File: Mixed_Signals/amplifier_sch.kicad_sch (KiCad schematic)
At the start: 6 parts, among them J1 audio connector, U1 ${SIM.PARAMS}

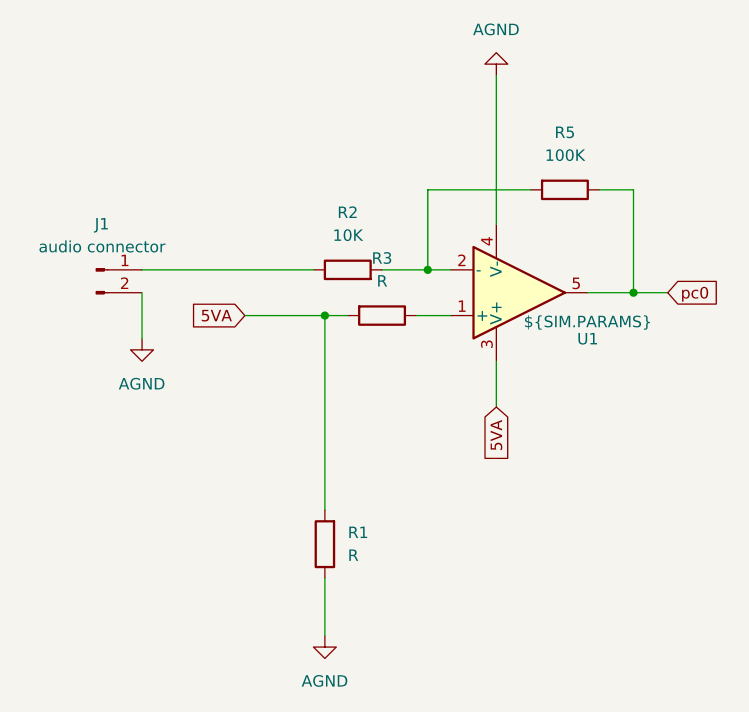
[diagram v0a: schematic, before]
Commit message: Fixed voltage divider error
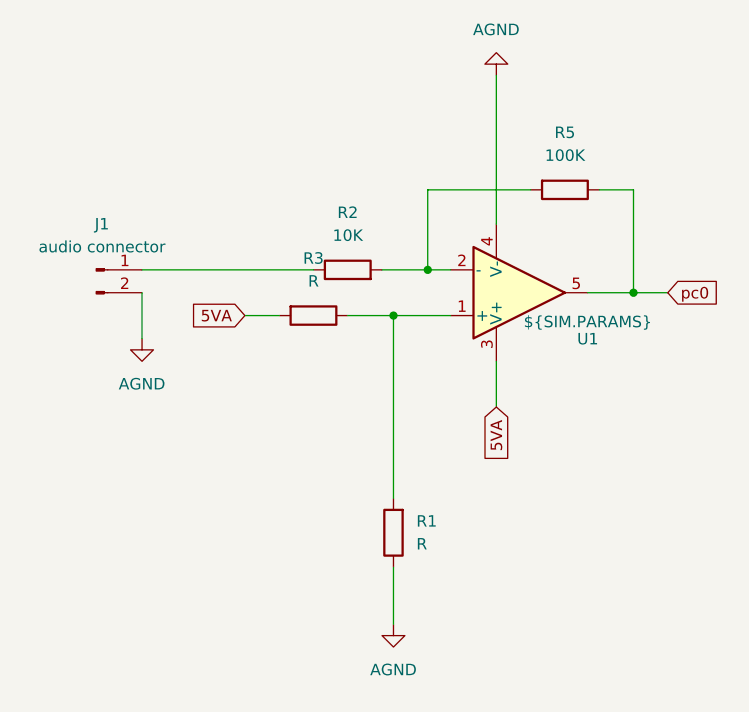
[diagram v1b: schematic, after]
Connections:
- net 5VA: no longer R1.2
- net at R3.1, U1.1 (+): now also R1.2
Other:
- moved on the sheet: R1, R3
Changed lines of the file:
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@@
 	(paper "A4")
 	(junction
-		(at 106.68 95.25)
+		(at 114.3 95.25)
 		(diameter 0)
 		(color 0 0 0 0)
@@
 	(wire
 		(pts
-			(xy 109.22 95.25) (xy 106.68 95.25)
-		)
-		(stroke
-			(width 0)
-			(type default)
-		)
-	)
-	(wire
-		(pts
 			(xy 125.73 85.09) (xy 125.73 68.58)
 		)
@@
 	(wire
 		(pts
-			(xy 116.84 95.25) (xy 120.65 95.25)
+			(xy 109.22 95.25) (xy 114.3 95.25)
 		)
 		(stroke
@@
 	(wire
 		(pts
-			(xy 106.68 124.46) (xy 106.68 130.81)
+			(xy 114.3 115.57) (xy 114.3 95.25)
+		)
+		(stroke
+			(width 0)
+			(type default)
+		)
+	)
+	(wire
+		(pts
+			(xy 114.3 95.25) (xy 120.65 95.25)
+		)
+		(stroke
+			(width 0)
+			(type default)
+		)
+	)
+	(wire
+		(pts
+			(xy 114.3 123.19) (xy 114.3 129.54)
 		)
 		(stroke
@@
 	(wire
 		(pts
-			(xy 97.79 95.25) (xy 106.68 95.25)
+			(xy 97.79 95.25) (xy 101.6 95.25)
 		)
 		(stroke
@@
 		(pts
 			(xy 129.54 81.28) (xy 118.11 81.28)
-		)
-		(stroke
-			(width 0)
-			(type default)
-		)
-	)
-	(wire
-		(pts
-			(xy 106.68 95.25) (xy 106.68 116.84)
 		)
 		(stroke
@@
 	(symbol
 		(lib_id "Device:R")
-		(at 113.03 95.25 270)
+		(at 105.41 95.25 270)
 		(unit 1)
 		(exclude_from_sim no)
@@
 		(fields_autoplaced yes)
 		(property "Reference" "R3"
-			(at 113.03 88.9 90)
+			(at 105.41 88.9 90)
 			(effects
 				(font
@@
 		)
 		(property "Value" "R"
-			(at 113.03 91.44 90)
+			(at 105.41 91.44 90)
 			(effects
 				(font
@@
 		)
 		(property "Footprint" "Resistor_SMD:R_0603_1608Metric"
-			(at 113.03 93.472 90)
+			(at 105.41 93.472 90)
 			(effects
 				(font
@@
 		)
 		(property "Datasheet" "~"
-			(at 113.03 95.25 0)
+			(at 105.41 95.25 0)
 			(effects
 				(font
@@
 		)
 		(property "Description" "Resistor"
-			(at 113.03 95.25 0)
+			(at 105.41 95.25 0)
 			(effects
 				(font
@@
 	(symbol
 		(lib_id "power:GND")
-		(at 106.68 130.81 0)
+		(at 114.3 129.54 0)
 		(unit 1)
 		(exclude_from_sim no)
@@
 		(fields_autoplaced yes)
 		(property "Reference" "#PWR03"
-			(at 106.68 137.16 0)
+			(at 114.3 135.89 0)
 			(effects
 				(font
@@
 		)
 		(property "Value" "AGND"
-			(at 106.68 135.89 0)
+			(at 114.3 134.62 0)
 			(effects
 				(font
@@
 		)
 		(property "Footprint" ""
-			(at 106.68 130.81 0)
+			(at 114.3 129.54 0)
 			(effects
 				(font
@@
 		)
 		(property "Datasheet" ""
-			(at 106.68 130.81 0)
+			(at 114.3 129.54 0)
 			(effects
 				(font
@@
 		)
 		(property "Description" "Power symbol creates a global label with name \"GND\" , ground"
-			(at 106.68 130.81 0)
+			(at 114.3 129.54 0)
 			(effects
 				(font
@@
 	(symbol
 		(lib_id "Device:R")
-		(at 106.68 120.65 180)
+		(at 114.3 119.38 180)
 		(unit 1)
 		(exclude_from_sim no)
@@
 		(fields_autoplaced yes)
 		(property "Reference" "R1"
-			(at 109.22 119.3799 0)
+			(at 116.84 118.1099 0)
 			(effects
 				(font
@@
 		)
 		(property "Value" "R"
-			(at 109.22 121.9199 0)
+			(at 116.84 120.6499 0)
 			(effects
 				(font
@@
 		)
 		(property "Footprint" "Resistor_SMD:R_0603_1608Metric"
-			(at 108.458 120.65 90)
+			(at 116.078 119.38 90)
 			(effects
 				(font
@@
 		)
 		(property "Datasheet" "~"
-			(at 106.68 120.65 0)
+			(at 114.3 119.38 0)
 			(effects
 				(font
@@
 		)
 		(property "Description" "Resistor"
-			(at 106.68 120.65 0)
-			(effects
-				(font
+			(at 114.3 119.38 0)
+			(effects
+				(font
